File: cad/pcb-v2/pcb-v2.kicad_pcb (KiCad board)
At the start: 2 copper layers, 19.6 x 17.6 mm, 2 parts, among them U1 ESP32-C3-MINI-1

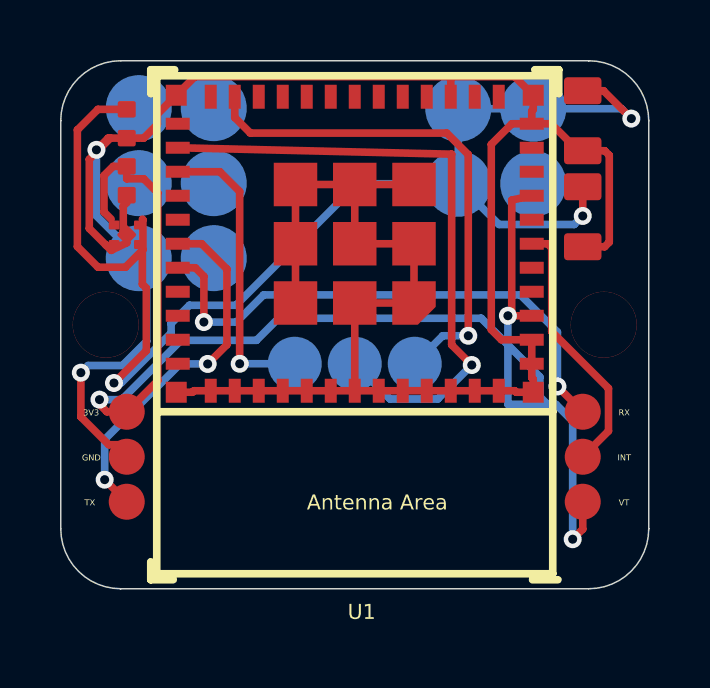
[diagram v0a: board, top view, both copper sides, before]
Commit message: WIP: U2 pads moved, local routing NOT yet corrected - board has a short
DO NOT PLOT GERBERS FROM THIS COMMIT.

Contains:
  - U2 land pattern corrected (commit 266390f, verified correct)
  - U1 pin 5 (GPIO2) tied to +3V3 by a 0.668 mm stub, 0.473 mm clearance, OK
  - check_board.py, a geometry checker that honours pad SHAPE

KNOWN BROKEN: moving U2's pads by ~0.2 mm left the existing tracks where they
were, drawn to the old pad positions. Result:

  SHORT  U2-1 (+3V3) touching a GND track   0.0000 mm
  tight  U2-5 (GND)  vs a VBAT track        0.0970 mm
  tight  U2-3 (VBAT) vs a GND track         0.1140 mm

The escape corridors around a 1x1 X2SON are under 0.5 mm, so the local tracks
need re-routing at reduced width, not just nudging. That is the next job.

Also corrected here: check_board.py previously modelled every pad as a
rectangle, which inflates a circular pad by up to 0.207*d at the corners
(0.46 mm on a 2.2 mm pogo pad) and produced eight false violations on J2/J4/
J11/TP. With shapes honoured, the as-imported board is clean: one pair at
0.1270 mm, exactly at the limit, not under it. Altium's DRC was right.
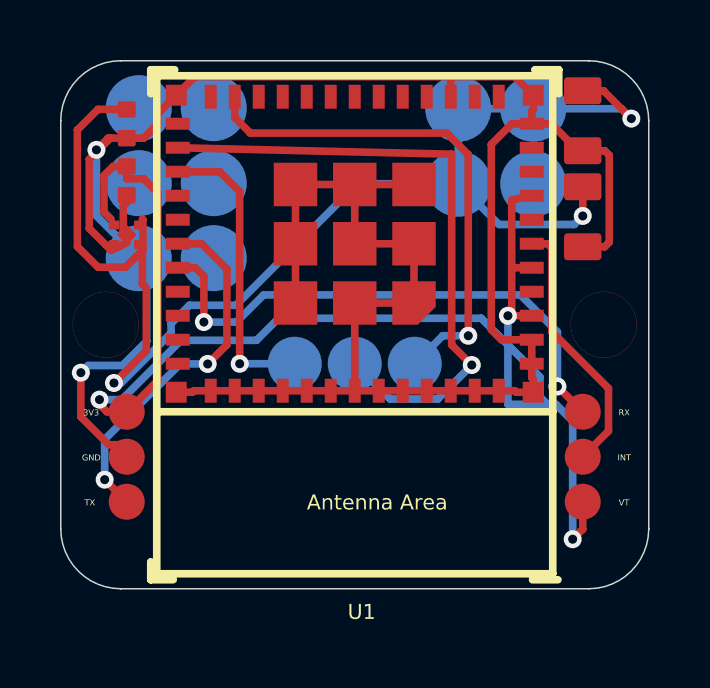
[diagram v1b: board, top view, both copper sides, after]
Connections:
- U1 pad 5: (no net) -> +3V3
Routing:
- net +3V3: track 46.6 -> 47.3 mm
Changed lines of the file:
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@@
 			(size 0.4 0.8)
 			(layers "F.Cu" "F.Mask" "F.Paste")
+			(net "+3V3")
 			(solder_mask_margin 0)
 		)
@@
 	)
 	(segment
+		(start 154.4011 103.1036)
+		(end 153.733 103.1036)
+		(width 0.254)
+		(layer "F.Cu")
+		(net "+3V3")
+	)
+	(segment
